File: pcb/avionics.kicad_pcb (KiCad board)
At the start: 2 copper layers, 100 x 48 mm, 112 parts, among them IC101 STM32F405VGT, IC102 ADP3335, IC201 MAX-7Q, IC701 ADXL345, IC702 L3G4200D, IC703 MS5611-01BA03, IC704 HMC5883L, M3_MOUNT VAL**, P101 CONN_01X02, P102 CONN_01X04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

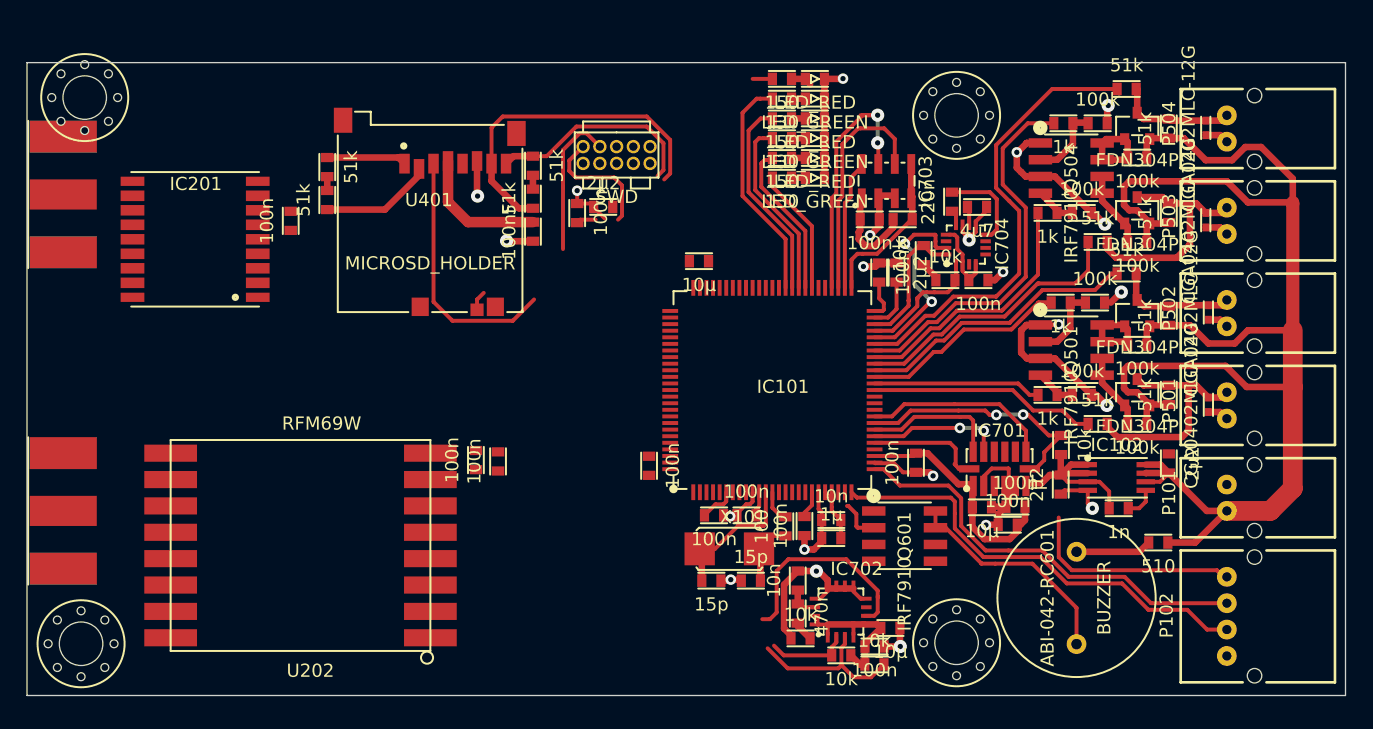
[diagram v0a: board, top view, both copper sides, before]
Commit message: I have moved the microcontroller to what I believe is the optumum position. I have also changed the transistor for the buzzer to a 300R resistor and the buzzer pin to pin 24 PA1. I had to reconnect all the capacitors since they appear to have shrinked when i opened them on my computer.
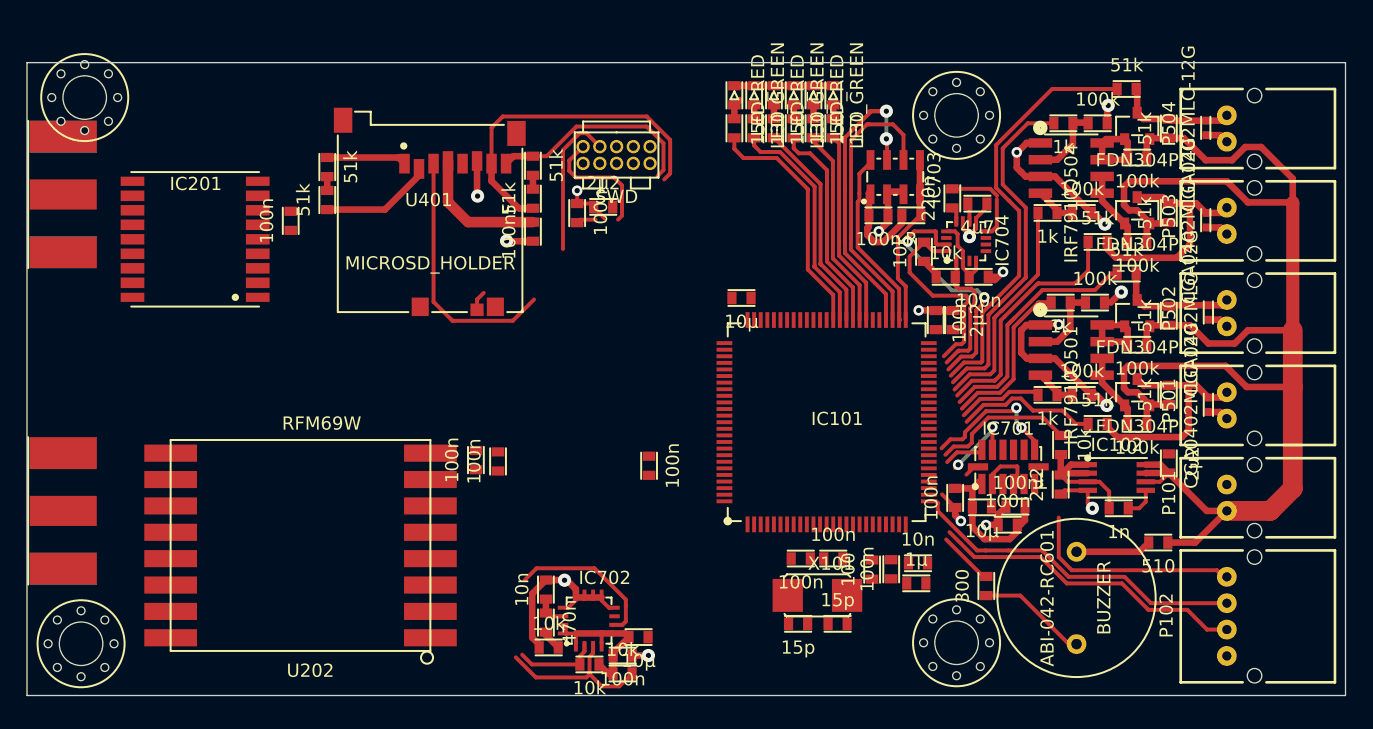
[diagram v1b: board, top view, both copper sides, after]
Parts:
- removed Q601: IRF7910, avionics14:SO-8
- added R608: 300, avionics14:0603, F.Cu at (160.8, 80.7)
- moved R701 19.1 mm to (130.7, 86.6)
- moved R704 19.1 mm to (127.6, 85.4)
- moved C702 19.1 mm to (134.4, 84.6)
- moved C704 19.1 mm to (133.2, 86.0)
- moved C706 19.1 mm to (127.4, 81.0)
- moved C707 19.1 mm to (127.4, 83.5)
- moved IC702 19.1 mm to (129.6, 85.1)
- moved R702 19.1 mm to (133.2, 87.3)
- moved X101 7.56 mm to (145.9, 81.4)
- moved C107 7.35 mm to (149.5, 83.6)
- moved C102 7.35 mm to (153.5, 79.4)
- moved C103 7.35 mm to (146.7, 78.6)
- moved C106 7.35 mm to (146.5, 83.6)
- moved C108 7.35 mm to (155.6, 79.0)
- moved C110 7.35 mm to (149.1, 78.6)
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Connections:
- IC101 pad 24: Net-(IC101-Pad24) -> /Datalogging & Pyros/BUZZER
- IC101 pad 56: /Datalogging & Pyros/BUZZER -> Net-(IC101-Pad56)
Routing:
- net +3V3: track 103.7 -> 80.1 mm
- net GND: track 112.5 -> 92.1 mm, vias 22 -> 17
- net /Datalogging & Pyros/~IMU_OK: track 1.50 -> 18.4 mm
- net Net-(C106-Pad1): track 10.4 -> 0.00 mm
- net /EXT_TX: track 34.0 -> 24.1 mm
- net Net-(ABI-042-RC601-Pad2): track 17.3 -> 8.37 mm
- net /Inertial Measurement/ACCEL_CS: track 19.3 -> 11.5 mm, vias 2 -> 0
- net /Inertial Measurement/ACCEL_SCK: track 9.08 -> 2.06 mm
- net /Inertial Measurement/ACCEL_MOSI: track 10.6 -> 3.61 mm
- net /EXT_RX: track 32.2 -> 25.6 mm
- net /Datalogging & Pyros/~PY1_CHK: track 17.7 -> 11.2 mm
- net /Datalogging & Pyros/PY1_TRG: track 12.8 -> 6.46 mm
- net /Datalogging & Pyros/PY_OK: track 9.59 -> 14.9 mm
- net Net-(C107-Pad1): track 5.06 -> 0.00 mm
- net /Inertial Measurement/MAGNO_SDA: track 10.8 -> 15.6 mm
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
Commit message: continued routing, note that we need to solve how to connect nReset and also how to power all the VDDs.
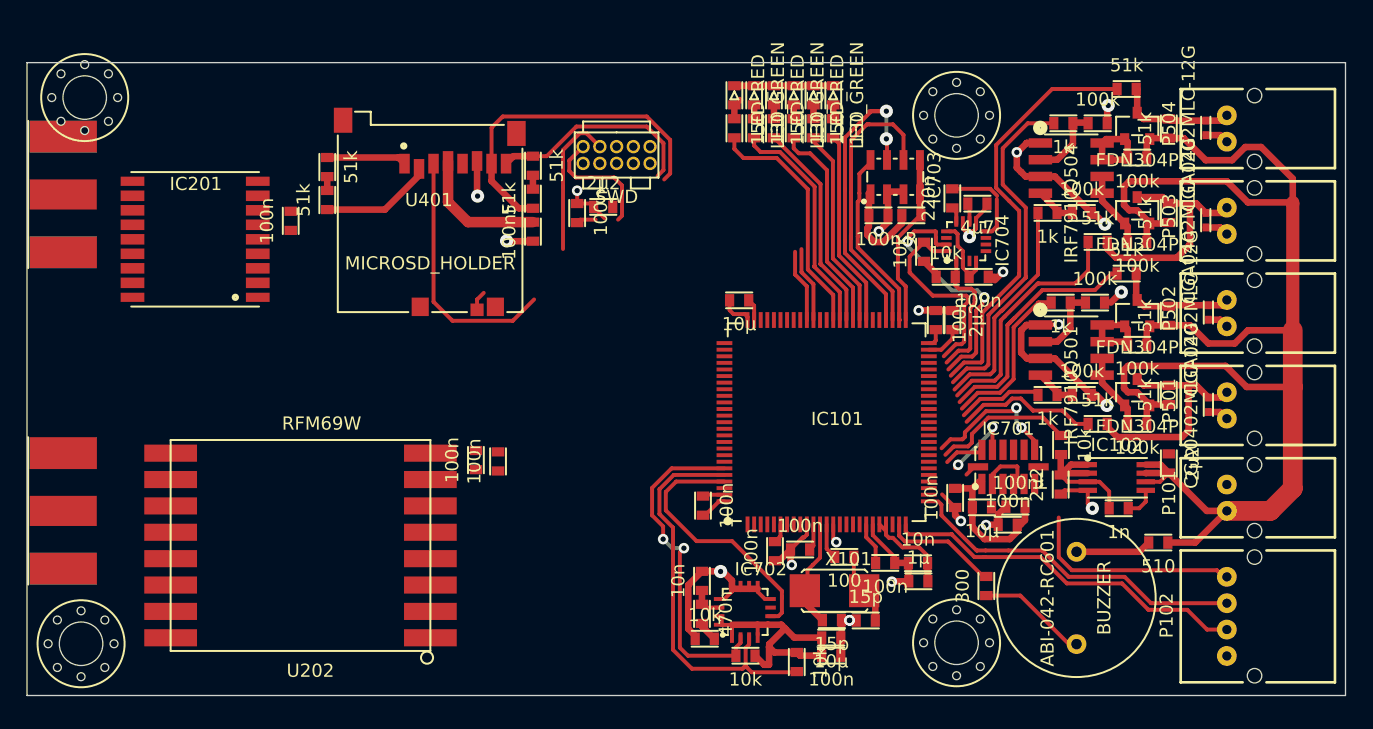
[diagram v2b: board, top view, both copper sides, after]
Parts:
- moved C704 15.8 mm to (149.0, 86.0)
- moved C702 14.6 mm to (149.0, 84.6)
- moved R702 13.2 mm to (146.4, 86.5), turned to 90 degrees
- moved R701 11.9 mm to (142.5, 86.0)
- moved R704 11.9 mm to (139.4, 84.7)
- moved IC702 11.9 mm to (141.5, 84.4)
- moved C706 11.9 mm to (139.2, 80.3)
- moved C707 11.9 mm to (139.2, 82.8)
- moved C109 5.09 mm to (139.3, 74.6)
- moved C110 2.61 mm to (146.6, 77.9)
- moved C106 2.58 mm to (149.0, 83.3)
- moved R101 2.32 mm to (150.0, 78.5), turned to 0 degrees
- moved C107 2.15 mm to (151.6, 83.3)
- moved C103 2.03 mm to (144.7, 78.1), turned to 270 degrees
- moved X101 1.34 mm to (147.2, 81.1)
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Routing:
- net +3V3: track 80.1 -> 109.0 mm
- net /Inertial Measurement/GYRO_SCL: track 6.40 -> 26.2 mm, vias 0 -> 2
- net GND: track 92.1 -> 110.6 mm, vias 17 -> 20
- net /Inertial Measurement/GYRO_SDA: track 12.8 -> 30.8 mm
- net /Inertial Measurement/GYRO_DRDY: track 11.8 -> 20.3 mm
- net Net-(C106-Pad1): track 0.00 -> 8.29 mm
- net Net-(C107-Pad1): track 0.00 -> 5.78 mm
- net /Datalogging & Pyros/µSD_DAT0: track 25.9 -> 31.6 mm
- net /Datalogging & Pyros/µSD_DAT1: track 16.3 -> 21.8 mm
- net /Datalogging & Pyros/BUZZER: track 4.21 -> 8.75 mm
- net /EXT_TX: track 24.1 -> 28.0 mm
- net Net-(C111-Pad1): track 0.00 -> 2.82 mm
- net Net-(IC101-Pad13): track 0.00 -> 2.77 mm
- net /nReset: track 0.00 -> 1.44 mm, vias 0 -> 1

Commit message: continued routing
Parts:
- moved R520 2.89 mm to (174.1, 44.1)
- moved R702 1.47 mm to (145.6, 85.2)
- moved R608 1.38 mm to (160.3, 79.4), turned to 0 degrees
- moved C110 1.22 mm to (145.4, 78.2), turned to 270 degrees
- moved C105 0.89 mm to (156.9, 59.6)
- moved C103 0.67 mm to (144.1, 78.2)
- moved C111 0.41 mm to (158.2, 60.1)
- moved R101 0.35 mm to (149.7, 78.7)
- moved C102 0.28 mm to (153.1, 78.7)
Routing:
- net +3V3: track 109.0 -> 283.5 mm, vias 0 -> 6
- net /nReset: track 1.44 -> 7.60 mm, vias 1 -> 0
- net /Datalogging & Pyros/~PY4_CHK: track 32.1 -> 36.1 mm
- net /Datalogging & Pyros/~PY1_CHK: track 11.2 -> 14.3 mm
- net /Datalogging & Pyros/PY1_TRG: track 6.46 -> 9.13 mm
- net /Datalogging & Pyros/PY2_TRG: track 13.4 -> 15.9 mm
- net /Datalogging & Pyros/~PY2_CHK: track 18.9 -> 21.2 mm
- net Net-(C711-Pad1): track 4.86 -> 7.16 mm
- net (no net): track 3.22 -> 0.92 mm
- net /Datalogging & Pyros/~PY3_CHK: track 18.4 -> 20.6 mm
- net /Datalogging & Pyros/PY3_TRG: track 17.0 -> 18.9 mm
- net /Inertial Measurement/MAGNO_DRDY: track 19.4 -> 21.2 mm
- net /Datalogging & Pyros/PY4_TRG: track 26.2 -> 27.9 mm
- net /Inertial Measurement/MAGNO_SDA: track 15.6 -> 17.3 mm
- net /Inertial Measurement/MAGNO_SCL: track 10.8 -> 12.2 mm
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
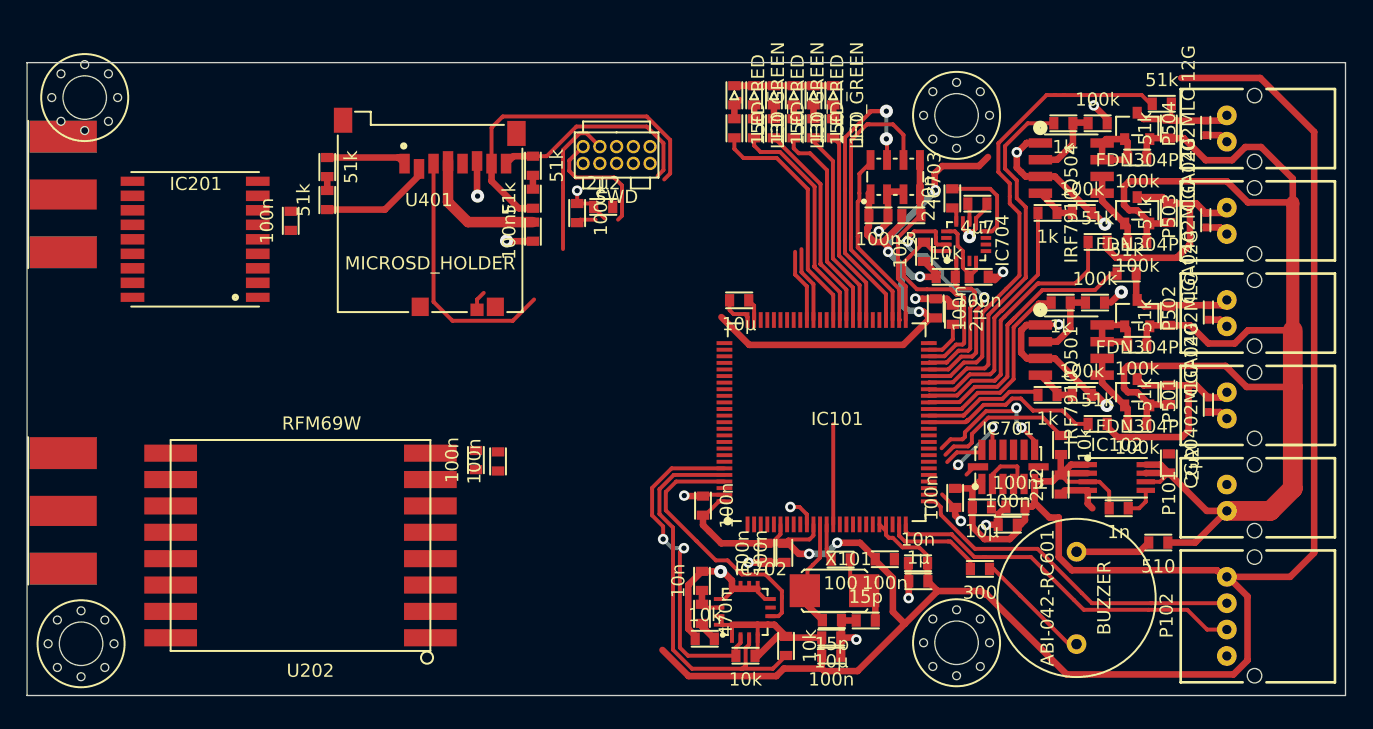
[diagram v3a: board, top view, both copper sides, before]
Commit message: tidied up some routing
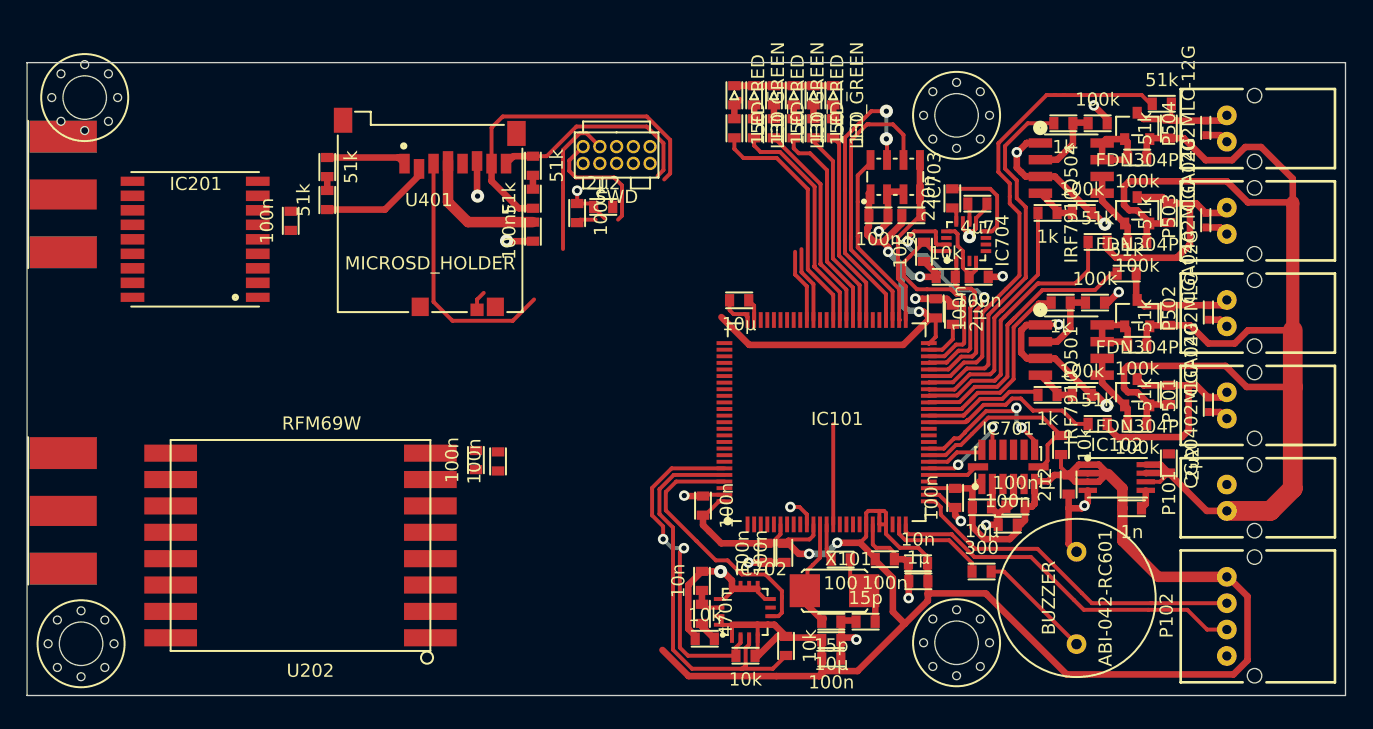
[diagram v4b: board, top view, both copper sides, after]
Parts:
- removed R607: 510, avionics14:0603
- moved C116 1.00 mm to (171.8, 74.8)
- moved C117 0.60 mm to (167.0, 73.0)
- moved R608 0.24 mm to (160.4, 79.6), turned to 180 degrees
- moved C704 0.22 mm to (149.0, 86.2)
- moved C702 0.19 mm to (149.0, 84.8)
- moved C106 0.12 mm to (149.0, 83.4)
- moved C107 0.09 mm to (151.6, 83.4)
- turned ABI-042-RC601 to 90 degrees
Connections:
- ABI-042-RC601 pad 2: Net-(ABI-042-RC601-Pad2) -> GND
- R608 pad 1: /Datalogging & Pyros/BUZZER -> Net-(ABI-042-RC601-Pad1)
- R608 pad 2: Net-(ABI-042-RC601-Pad2) -> /Datalogging & Pyros/BUZZER
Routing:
- net +3V3: track 283.5 -> 227.9 mm, vias 6 -> 5
- net GND: track 110.2 -> 121.2 mm, vias 20 -> 22
- net Net-(ABI-042-RC601-Pad2): track 8.96 -> 0.00 mm
- net +BATT: track 115.0 -> 109.6 mm
- net /Inertial Measurement/ACCEL_CS: track 11.5 -> 16.0 mm
- net /Inertial Measurement/ACCEL_SCK: track 2.06 -> 5.41 mm
- net Net-(ABI-042-RC601-Pad1): track 5.76 -> 8.75 mm
- net /Inertial Measurement/ACCEL_MISO: track 6.22 -> 8.22 mm
- net /Inertial Measurement/ACCEL_MOSI: track 3.61 -> 4.99 mm
- net /Inertial Measurement/BARO_MOSI: track 24.3 -> 23.0 mm
- net (no net): track 0.92 -> 0.00 mm, vias 1 -> 0
- net Net-(C116-Pad2): track 2.39 -> 1.49 mm
- net /Inertial Measurement/ACCEL_INT: track 11.1 -> 11.9 mm

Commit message: tidied some more stuff
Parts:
- moved P103 16.2 mm to (144.8, 54.4), turned to 180 degrees
- moved C114 11.9 mm to (140.0, 58.4)
- moved C113 11.8 mm to (142.0, 57.6)
- moved C203 9.78 mm to (114.4, 74.2)
- moved C204 7.65 mm to (114.6, 69.4), turned to 0 degrees
- moved U202 3.56 mm to (121.0, 67.0)
- moved C401 2.00 mm to (127.6, 52.2)
- moved R401 2.00 mm to (127.6, 49.7)
- moved R402 2.00 mm to (127.6, 47.2)
- moved R403 2.00 mm to (112.0, 47.3)
- moved R404 2.00 mm to (112.0, 49.8)
- moved U401 1.96 mm to (126.8, 58.4)
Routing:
- net /nReset: track 7.60 -> 35.7 mm, vias 0 -> 2
- net /Datalogging & Pyros/µSD_CMD: track 19.4 -> 0.00 mm
- net +3V3: track 227.9 -> 211.3 mm, vias 5 -> 6
- net /Radio/RX: track 0.00 -> 14.6 mm, vias 0 -> 2
- net /Radio/TX: track 0.00 -> 13.5 mm, vias 0 -> 2
- net /Radio/GPS_nRST: track 0.00 -> 11.9 mm, vias 0 -> 2
- net /Datalogging & Pyros/µSD_DAT0: track 31.6 -> 20.7 mm
- net /Datalogging & Pyros/µSD_DAT1: track 21.8 -> 16.8 mm
- net Net-(C113-Pad1): track 0.14 -> 3.30 mm
- net /SWDIO: track 9.45 -> 6.39 mm
- net GND: track 121.2 -> 122.5 mm
- net /SWDCLK: track 11.3 -> 12.5 mm

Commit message: yet more routing done!
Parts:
- moved R404 21.9 mm to (131.4, 60.0), turned to 0 degrees
- moved R403 21.1 mm to (128.8, 60.0), turned to 180 degrees
- moved C203 19.3 mm to (132.5, 67.6), turned to 90 degrees
- moved IC201 16.8 mm to (112.4, 46.4)
- moved C204 16.6 mm to (131.1, 67.6), turned to 90 degrees
- moved R401 12.9 mm to (140.2, 47.0)
- moved R402 12.9 mm to (140.2, 49.6)
- moved C401 11.2 mm to (138.6, 50.2)
- moved U401 10.6 mm to (137.4, 58.8)
- moved U202 9.45 mm to (130.3, 68.7)
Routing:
- net /Radio/RADIO_CLK: track 0.00 -> 66.0 mm, vias 0 -> 2
- net /Radio/RADIO_MISO: track 0.00 -> 59.4 mm
- net /Radio/RADIO_MOSI: track 0.00 -> 56.8 mm, vias 0 -> 2
- net +3V3: track 211.3 -> 267.1 mm, vias 6 -> 8
- net /Radio/RADIO_CS: track 0.00 -> 52.7 mm
- net /Datalogging & Pyros/µSD_CMD: track 0.00 -> 32.5 mm
- net /Radio/GPS_nRST: track 11.9 -> 41.8 mm
- net /Datalogging & Pyros/µSD_DAT3: track 8.53 -> 34.1 mm, vias 0 -> 2
- net /Datalogging & Pyros/µSD_DAT2: track 6.05 -> 31.4 mm, vias 0 -> 2
- net /Radio/RX: track 14.6 -> 39.2 mm
- net /Radio/TX: track 13.5 -> 36.8 mm
- net /Radio/RADIO_IRQ: track 0.00 -> 23.2 mm
- net /Datalogging & Pyros/µSD_CLK: track 0.00 -> 20.8 mm, vias 0 -> 2
- net /Datalogging & Pyros/µSD_DAT0: track 20.7 -> 29.5 mm
- net /Datalogging & Pyros/µSD_CD: track 1.50 -> 10.0 mm
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
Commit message: Almost done. Just in case
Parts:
- moved C201 15.2 mm to (120.9, 44.9), turned to 0 degrees
- moved P201 11.0 mm to (101.2, 54.5)
- moved P202 11.0 mm to (101.2, 71.7)
- moved M3_MOUNT 10.4 mm to (102.5, 85.0)
- moved M3_MOUNT 10.2 mm to (102.5, 45.0)
- moved C710 0.65 mm to (160.6, 51.3)
- moved C711 0.31 mm to (158.1, 51.0)
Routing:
- net +3V3: track 267.1 -> 419.8 mm, vias 8 -> 17
- net GND: track 126.3 -> 225.1 mm, vias 24 -> 33
- net Net-(IC201-Pad11): track 0.00 -> 16.0 mm
- net Net-(P202-Pad1): track 0.00 -> 9.40 mm
- net Net-(C711-Pad1): track 7.16 -> 9.30 mm
- net Net-(C710-Pad1): track 1.63 -> 2.13 mm
- net /Radio/GPS_nRST: track 41.8 -> 42.1 mm, vias 2 -> 4
- added copper zone on B.Cu, net GND
- added copper zone on F.Cu, net GND
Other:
- board size 100 x 48 mm -> 89.5 x 48 mm
